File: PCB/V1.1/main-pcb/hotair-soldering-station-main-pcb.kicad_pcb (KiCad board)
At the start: 2 copper layers, 89.4 x 90.9 mm, 93 parts, among them J1 230VAC_IN, J10 PB6, J11 PB4, J13 ICP (goldpin r2,54), J2 main-board-conn, J3 EARTH_GND, J4 24V_IN (NS-25 r2,54), J5 PSUPPLY (PWZ-02S r.3,96), J6 HOTAIR_FAN (JST r,2,54), J7 HOTAIR_MEAS (JST r.2,5), J8 HOTAIR_HEATER (PWZ-02S r.3,96), J9 SOLD_IRON (r.2,54), Q1 BC817, Q2 BC817, Q3 BC327, Q6 BT139-600, Q7 BC817, Q8 FP3055LP, Q9 BC817, U1 MOC3041M, U2 LMV324, U3 MP1584-Step-Down, U4 AP1117-ADJ, U5 STM32F030K6Tx, U6 DS18B20

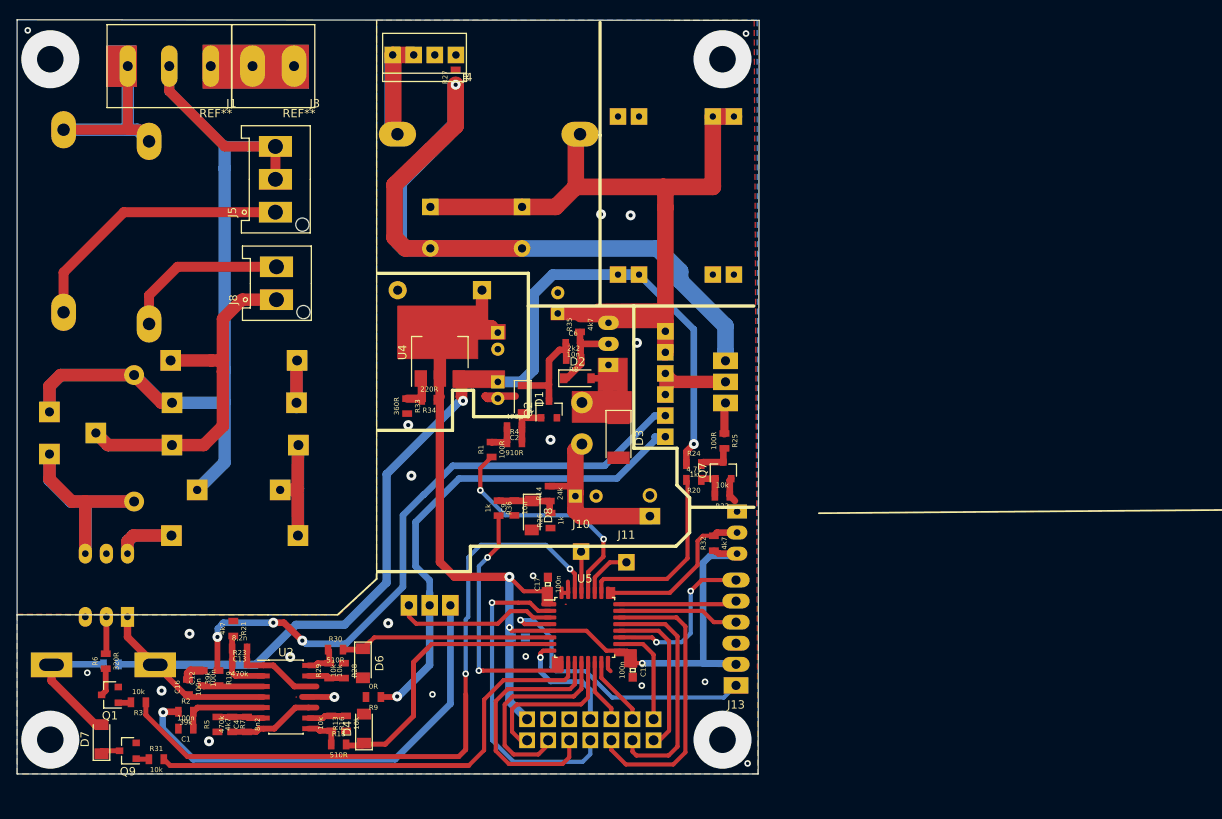
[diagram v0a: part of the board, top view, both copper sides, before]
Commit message: HV circuit resistor change, update footprints
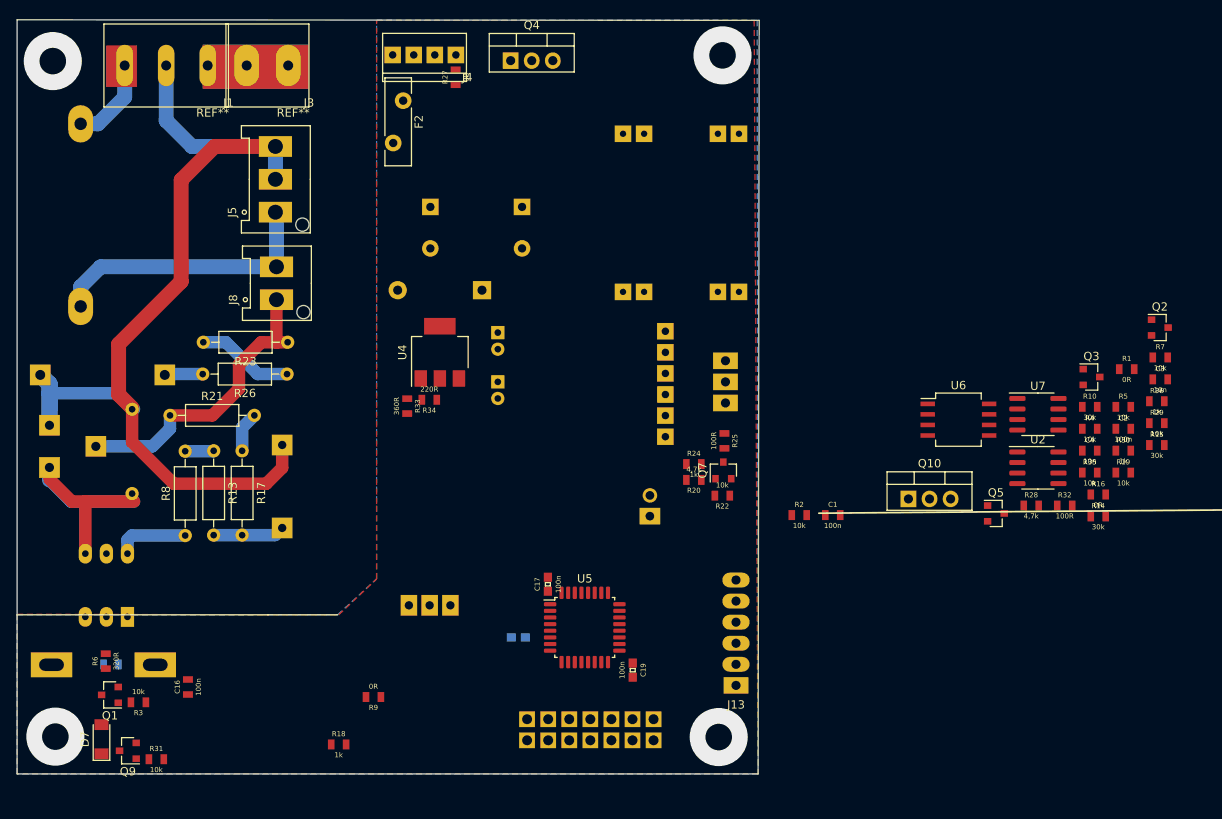
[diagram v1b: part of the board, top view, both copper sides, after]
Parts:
- removed C12: 100n, Capacitors:0805
- removed C13: 8,2n, Capacitors:0805
- removed C6, C9: 10n, Capacitors:0805
- removed C8: 47u/35V, Capacitor_THT:CP_Radial_D6.3mm_P2.50mm
- removed D1, D2: MBR052, Diodes_SMD:D_SOD-123
- removed D3: 1N5819, Diode_SMD:D_MELF
- removed D4, D8: 3V6, Diodes_SMD:D_MiniMELF
- removed D6: 3v6, Diodes_SMD:D_MiniMELF
- removed F3: Fuse, Fuse_Holders_and_Fuses:Fuseholder5x20_horiz_SemiClosed_Casing10x25mm
- removed J10: PB6, My-Footprints:WIRE_PAD_1,3mm
- removed J11: PB4, My-Footprints:WIRE_PAD_1,3mm
- removed L1: 220uH, Inductors_THT:L_Radial_D10.0mm_P5.00mm_Fastron_07M
- added Q10: FP3055LP, Package_TO_SOT_THT:TO-220-3_Vertical, F.Cu at (124.4, 75.7)
- added Q4: FP3055LP, Package_TO_SOT_THT:TO-220-3_Vertical, F.Cu at (76.5, 22.9)
- added Q5: BC817, Package_TO_SOT_SMD:SOT-23, F.Cu at (135.0, 77.4)
- added U7: MAX31855KASA, Package_SO:SOIC-8_3.9x4.9mm_P1.27mm, F.Cu at (140.0, 65.5)
- C2: value 470p -> 100n
- C3: value 100u/35V -> 10n; footprint Capacitor_THT:CP_Radial_D6.3mm_P2.50mm -> Capacitors:0805; moved to F.Cu
- C4: value 8n2 -> 10n
- F1: value Fuse -> 3,15A
- F2: value Fuse -> Polyfuse; footprint Fuse_Holders_and_Fuses:Fuseholder5x20_horiz_SemiClosed_Casing10x25mm -> Fuse:Fuse_Bourns_MF-RG500; moved to F.Cu
- Q2: value BC817 -> BC807
- Q3: value BC327 -> BC817; footprint My-Footprints:TO-92_Inline_Wide -> Package_TO_SOT_SMD:SOT-23; moved to F.Cu
- R1: value 100R -> 0R
- R10, R15: value 2x390R -> 30k; footprint Resistor_THT:R_Axial_DIN0414_L11.9mm_D4.5mm_P15.24mm_Horizontal -> Capacitors:0805; moved to F.Cu
- R12: footprint Resistor_THT:R_Axial_DIN0414_L11.9mm_D4.5mm_P15.24mm_Horizontal -> Resistors_ThroughHole:R_Axial_DIN0207_L6.3mm_D2.5mm_P10.16mm_Horizontal
- R13: value 10k -> 200R; footprint Capacitors:0805 -> Resistors_ThroughHole:R_Axial_DIN0207_L6.3mm_D2.5mm_P10.16mm_Horizontal
- R14: value 24k -> 30k
- R16: value 10k -> 0R
- R17: value 100R -> 200R; footprint Resistor_THT:R_Axial_DIN0414_L11.9mm_D4.5mm_P15.24mm_Horizontal -> Resistors_ThroughHole:R_Axial_DIN0207_L6.3mm_D2.5mm_P10.16mm_Horizontal; moved to F.Cu
- R18, R30: value 510R -> 1k
- R19, R2: value 39k -> 10k
- R21: value 4k7 -> 200R; footprint Capacitors:0805 -> Resistors_ThroughHole:R_Axial_DIN0207_L6.3mm_D2.5mm_P10.16mm_Horizontal
- R23: value 470k -> 50R; footprint Capacitors:0805 -> Resistors_ThroughHole:R_Axial_DIN0207_L6.3mm_D2.5mm_P10.16mm_Horizontal
- R26: value 1k -> 50R; footprint Capacitors:0805 -> Resistors_ThroughHole:R_Axial_DIN0207_L6.3mm_D2.5mm_P10.16mm_Horizontal
- R28: value 10k -> 4,7k
- R32: value 4k7 -> 100R
- R35, R5: value 4k7 -> 10k
- R4: value 910R -> 10k
- R7: value 470k -> 10k
- R8: value 2k2 -> 200R; footprint Capacitors:0805 -> Resistors_ThroughHole:R_Axial_DIN0207_L6.3mm_D2.5mm_P10.16mm_Horizontal
- U2: value LMV324 -> MAX31855KASA; footprint Housings_SOIC:SOIC-14_3.9x8.7mm_Pitch1.27mm -> Package_SO:SOIC-8_3.9x4.9mm_P1.27mm
- U6: value DS18B20 -> LM358; footprint My-Footprints:TO-92_Inline_Wide -> Housings_SOIC:SO-8_5.3x6.2mm_Pitch1.27mm; moved to F.Cu
- moved R7 120.3 mm to (154.8, 58.6), turned to 0 degrees
- moved R5 115.7 mm to (150.3, 64.6), turned to 0 degrees
- moved R19 111.8 mm to (150.3, 72.5), turned to 0 degrees
- moved R10 111.7 mm to (146.3, 64.6)
- moved C4 106.8 mm to (146.3, 69.9), turned to 0 degrees
- moved R29 104.1 mm to (154.3, 66.6), turned to 0 degrees
- moved R15 103.4 mm to (154.3, 69.2), turned to 0 degrees
- moved R30 97.9 mm to (150.3, 69.9)
- moved R16 96.4 mm to (147.3, 75.2), turned to 0 degrees
- moved U2 94.7 mm to (140.0, 71.9)
- moved R28 85.2 mm to (139.2, 76.5), turned to 0 degrees
- moved C1 82.1 mm to (115.3, 77.6), turned to 0 degrees
- moved R36 80.3 mm to (154.3, 63.9), turned to 0 degrees
- moved R2 77.6 mm to (111.3, 77.6)
- moved R1 77.1 mm to (150.7, 60.1), turned to 0 degrees
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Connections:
- net 7SEG_DIN renamed SPI1_MOSI
- net Net-(C14-Pad2) renamed 3.3V
- net SOLDERING_IRON_HEATER_GND renamed IRON_WEP_HEATER
- net SOLD_IRON_HEATER_CTRL renamed IRON_WEP_HEATER_CTRL
- net THERM_HOTAIR_ADC renamed HOTAIR_ADC
- C2 pad 1: Net-(C2-Pad1) -> FAN_ADC
- C2 pad 2: Net-(C2-Pad2) -> GND
- C3 pad 1: +24V -> Net-(C3-Pad1)
- C4 pad 1: Net-(C4-Pad1) -> IRON_T12_THERM
- C4 pad 2: Net-(C4-Pad2) -> GND
- F1 pad 1: Net-(F1-Pad1) -> AC_230(L)
- F1 pad 2: AC_230(L) -> Net-(F1-Pad2)
- J1 pad 3: AC_230(L) -> Net-(F1-Pad2)
- J2 pad 12: 7SEG_CLK -> SPI1_SCK
- J2 pad 13: 7SEG_LATCH -> (no net)
- J5 pad 1: Net-(F1-Pad1) -> AC_230(L)
- J8 pad 2: Net-(F3-Pad2) -> AC_230(L)
- J9 pad 5: SOLDERING_IRON_THERM -> IRON_WEP_THERM
- Q2 pad 1: Net-(C2-Pad1) -> Net-(C1-Pad1)
- Q2 pad 2: GND -> Net-(Q2-Pad2)
- Q2 pad 3: Net-(C6-Pad1) -> GND
- Q3 pad 1: Net-(D2-Pad2) -> Net-(Q2-Pad2)
- Q3 pad 2: Net-(C6-Pad2) -> Net-(Q3-Pad2)
- Q3 pad 3: +24V -> Net-(Q3-Pad3)
- R1 pad 1: FAN_PWM -> HOTAIR_THERM
- R1 pad 2: Net-(C2-Pad2) -> Net-(R1-Pad2)
- R10 pad 1: Net-(R10-Pad1) -> FAN_SUPPLY
- R10 pad 2: Net-(C5-Pad1) -> Net-(Q3-Pad2)
- R13 pad 1: GND -> Net-(R13-Pad1)
- R13 pad 2: Net-(R13-Pad2) -> Net-(C5-Pad1)
- R14 pad 1: Net-(C9-Pad2) -> FAN_ADC
- R15 pad 1: Net-(C5-Pad1) -> GND
- R15 pad 2: Net-(J8-Pad1) -> FAN_ADC
- R16 pad 1: Net-(R13-Pad2) -> HOTAIR_THERM
- R16 pad 2: Net-(R16-Pad2) -> Net-(C3-Pad1)
- R17 pad 1: Net-(J8-Pad1) -> Net-(R17-Pad1)
- R17 pad 2: Net-(C7-Pad1) -> Net-(C5-Pad1)
- R18 pad 1: Net-(R16-Pad2) -> Net-(R18-Pad1)
- R19 pad 1: SOLDERING_IRON_THERM -> +3V3
- R19 pad 2: Net-(C12-Pad1) -> Net-(C3-Pad1)
- R2 pad 1: HOTAIR_THERM -> FAN_PWM
- R21 pad 1: GND -> Net-(J8-Pad1)
- R21 pad 2: Net-(C13-Pad2) -> Net-(R17-Pad1)
- R23 pad 1: Net-(C13-Pad2) -> Net-(J8-Pad1)
- R23 pad 2: Net-(C13-Pad1) -> Net-(R23-Pad2)
- R26 pad 1: GND -> Net-(R23-Pad2)
- R26 pad 2: Net-(C9-Pad2) -> Net-(C7-Pad1)
- R28 pad 1: GND -> Net-(Q5-Pad1)
- R28 pad 2: Net-(R28-Pad2) -> IRON_T12_HEATER_CTRL
- R29 pad 1: Net-(R28-Pad2) -> GND
- R29 pad 2: Net-(R29-Pad2) -> Net-(Q5-Pad1)
- R30 pad 1: Net-(R29-Pad2) -> +5V
- R30 pad 2: THERM_IRON_ADC -> Net-(Q5-Pad3)
- R32 pad 1: +3V3 -> Net-(Q10-Pad1)
- R32 pad 2: Net-(R32-Pad2) -> Net-(Q5-Pad3)
- R35 pad 1: Net-(C6-Pad2) -> +3V3
- R35 pad 2: +24V -> IRON_T12_THERM
- R36 pad 1: Net-(C9-Pad2) -> Net-(R36-Pad1)
- R36 pad 2: FAN_ADC -> IRON_T12_ADC
- R4 pad 1: Net-(C2-Pad2) -> +24V
- R4 pad 2: Net-(C2-Pad1) -> Net-(Q2-Pad2)
- R5 pad 1: GND -> +24V
- R5 pad 2: Net-(C4-Pad2) -> Net-(Q3-Pad3)
- R7 pad 1: Net-(C4-Pad2) -> Net-(Q3-Pad2)
- R7 pad 2: Net-(C4-Pad1) -> GND
- R8 pad 1: Net-(C6-Pad2) -> Net-(R8-Pad1)
- R8 pad 2: Net-(C6-Pad1) -> Net-(R13-Pad1)
- U1 pad 6: Net-(R10-Pad1) -> Net-(R8-Pad1)
- U2 pad 1: Net-(C13-Pad1) -> GND
- U2 pad 2: Net-(C13-Pad2) -> THERM_GND
- U2 pad 3: Net-(C12-Pad1) -> Net-(R1-Pad2)
- U2 pad 4: +5V -> +3V3
- U2 pad 5: Net-(C1-Pad1) -> SPI1_SCK
- U2 pad 6: Net-(C4-Pad2) -> MAX31855_HOTAIR_CS
- U2 pad 7: Net-(C4-Pad1) -> SPI1_MISO
- U2 pad 8: Net-(R16-Pad2) -> (no net)
- U5 pad 11: 7SEG_CLK -> SPI1_SCK
- U5 pad 12: 7SEG_LATCH -> SPI1_MISO
- U5 pad 25: Net-(R32-Pad2) -> IRON_T12_HEATER_CTRL
- U5 pad 27: Net-(J11-Pad1) -> (no net)
- U5 pad 29: Net-(J10-Pad1) -> MAX31855_HOTAIR_CS
- U5 pad 6: THERM_IRON_ADC -> IRON_T12_ADC
- U6 pad 1: GND -> Net-(R18-Pad1)
- U6 pad 2: Net-(R32-Pad2) -> Net-(R18-Pad1)
- U6 pad 3: +3V3 -> Net-(C3-Pad1)
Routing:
- net +5V: track 148.7 -> 0.00 mm, vias 2 -> 0
- net +3V3: track 131.8 -> 0.00 mm, vias 3 -> 0
- net 3.3V: track 107.6 -> 0.00 mm, vias 1 -> 0
- net +24V: track 88.1 -> 0.00 mm
- net HOTAIR_HEATER_CTRL: track 83.0 -> 0.00 mm, vias 2 -> 0
- net SOLDERING_IRON_THERM: track 76.8 -> 0.00 mm, vias 3 -> 0
- net THERM_GND: track 62.3 -> 0.00 mm, vias 1 -> 0
- net BUZZER: track 58.8 -> 0.00 mm
- net HOTAIR_THERM: track 54.7 -> 0.00 mm, vias 1 -> 0
- net SOLDER_ON_SW: track 39.0 -> 0.00 mm, vias 1 -> 0
- net RST: track 36.3 -> 0.00 mm, vias 1 -> 0
- net HOTAIR_ON_SW: track 35.0 -> 0.00 mm
- net HOTAIR_ADC: track 33.4 -> 0.00 mm
- net Net-(F1-Pad1): track 33.3 -> 0.00 mm
- net FAN_ADC: track 31.9 -> 0.00 mm, vias 2 -> 0
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
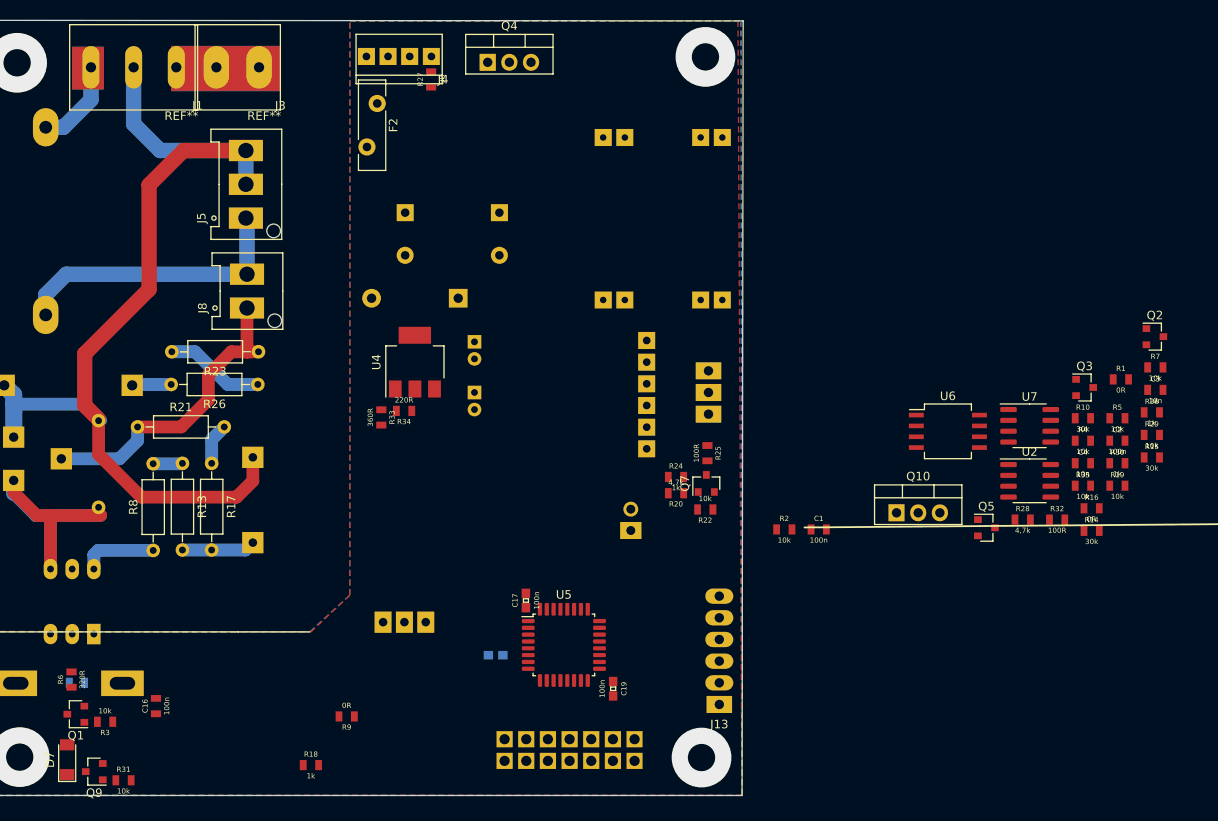
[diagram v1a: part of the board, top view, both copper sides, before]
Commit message: Main board routing, remove old 7seg from front panel schematic
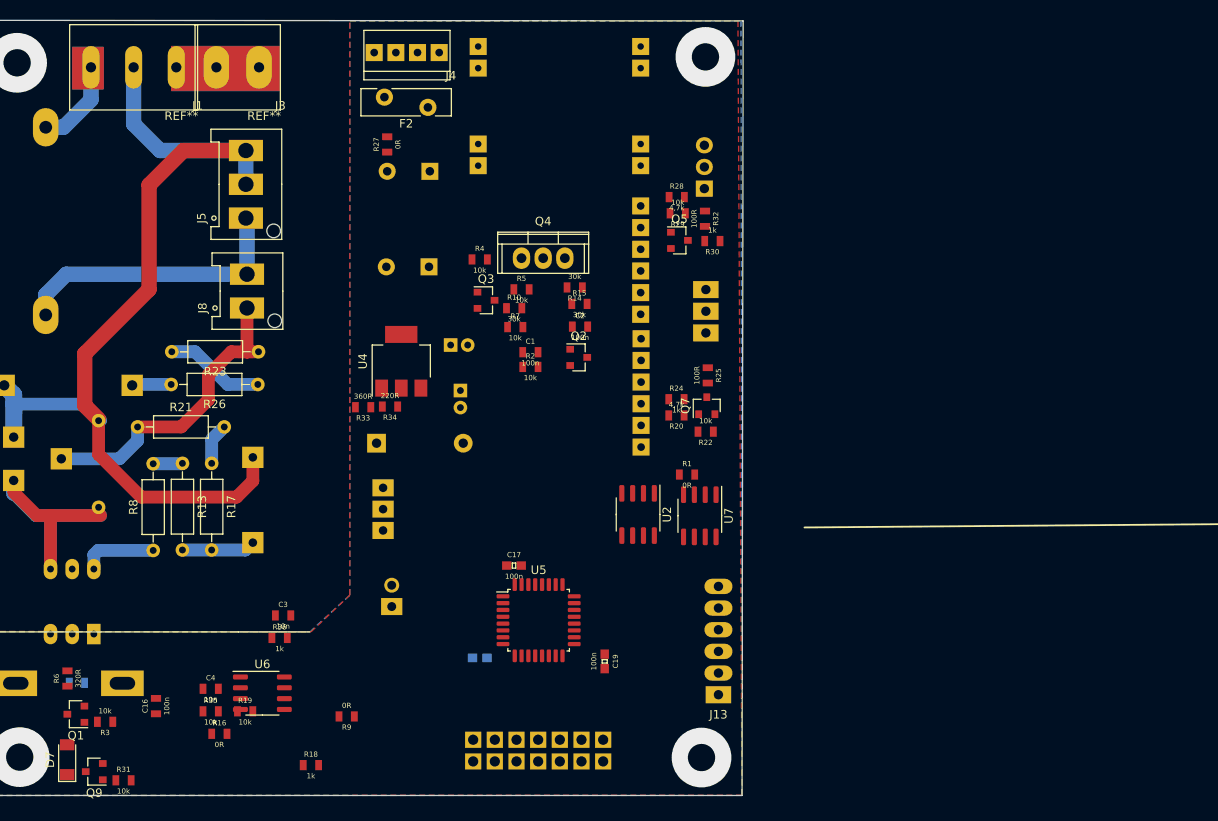
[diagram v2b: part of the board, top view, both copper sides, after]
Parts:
- added J10: SOLD_IRON (r.2,54), My-Footprints:Conn_1x06, B.Cu at (91.2, 38.5)
- C14, C15: footprint Capacitors_THT:CP_Radial_D10.0mm_P5.00mm -> Capacitors_ThroughHole:CP_Radial_D10.0mm_P5.00mm
- Q10: moved to B.Cu
- Q4: value FP3055LP -> Q_PMOS_GDS; footprint Package_TO_SOT_THT:TO-220-3_Vertical -> Power_Integrations:TO-220
- U6: footprint Housings_SOIC:SO-8_5.3x6.2mm_Pitch1.27mm -> Package_SO:SO-8_3.9x4.9mm_P1.27mm
- moved C4 105.6 mm to (44.0, 96.3)
- moved R19 105.6 mm to (48.0, 99.0)
- moved R35 105.6 mm to (44.0, 99.0)
- moved R36 105.6 mm to (52.1, 90.4)
- moved C3 105.6 mm to (52.5, 87.7)
- moved R16 105.6 mm to (45.0, 101.6)
- moved U6 86.0 mm to (50.1, 96.9)
- moved R7 75.2 mm to (79.7, 53.9)
- moved R4 73.8 mm to (75.5, 46.0)
- moved R5 71.5 mm to (80.4, 49.5)
- moved Q3 70.9 mm to (76.3, 50.8)
- moved R15 69.5 mm to (87.2, 51.2)
- moved R10 67.9 mm to (79.6, 51.7)
- moved Q2 67.6 mm to (87.1, 57.5)
- moved R14 67.0 mm to (86.7, 49.3), turned to 180 degrees
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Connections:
- net 3.3V renamed GND2
- Q10 pad 2: (no net) -> IRON_T12_HEATER
- Q4 pad 2: FAN_SUPPLY -> +24V
- Q4 pad 3: +24V -> FAN_SUPPLY
- U5 pad 25: IRON_T12_HEATER_CTRL -> MAX31855_HOTAIR_CS
- U5 pad 26: IRON_WEP_HEATER_CTRL -> (no net)
- U5 pad 27: (no net) -> IRON_WEP_HEATER_CTRL
- U5 pad 29: MAX31855_HOTAIR_CS -> IRON_T12_HEATER_CTRL

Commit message: uC change to STM32F103
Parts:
- added U8: STM32F103C6Tx, Package_QFP:LQFP-48_7x7mm_P0.5mm, F.Cu at (94.6, 86.5)
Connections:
- U5 pad 1: +3V3 -> (no net)
- U5 pad 10: BUZZER -> (no net)
- U5 pad 11: SPI1_SCK -> (no net)
- U5 pad 12: SPI1_MISO -> (no net)
- U5 pad 13: SPI1_MOSI -> (no net)
- U5 pad 14: SOLDER_UP_SW -> (no net)
- U5 pad 15: HOTAIR_DOWN_SW -> (no net)
- U5 pad 16: GND -> (no net)
- U5 pad 17: +3V3 -> (no net)
- U5 pad 18: HOTAIR_UP_SW -> (no net)
- U5 pad 19: UART_DBG_TX -> (no net)
- U5 pad 2: SOLDER_ON_SW -> (no net)
- U5 pad 20: HOTAIR_FAN_UP_SW -> (no net)
- U5 pad 21: HOTAIR_FAN_DOWN_SW -> (no net)
- U5 pad 22: HOTAIR_ON_SW -> (no net)
- U5 pad 23: SWDIO -> (no net)
- U5 pad 24: SWCLK -> (no net)
- U5 pad 25: MAX31855_HOTAIR_CS -> (no net)
- U5 pad 27: IRON_WEP_HEATER_CTRL -> (no net)
- U5 pad 28: FAN_PWM -> (no net)
- U5 pad 29: IRON_T12_HEATER_CTRL -> (no net)
- U5 pad 3: HOTAIR_REED_SW -> (no net)
- U5 pad 30: HOTAIR_HEATER_CTRL -> (no net)
- U5 pad 31: GND -> (no net)
- U5 pad 32: GND -> (no net)
- U5 pad 4: RST -> (no net)
- U5 pad 5: +3V3 -> (no net)
- U5 pad 6: IRON_T12_ADC -> (no net)
- U5 pad 7: HOTAIR_ADC -> (no net)
- U5 pad 8: SOLDER_DOWN_SW -> (no net)
- U5 pad 9: FAN_ADC -> (no net)
